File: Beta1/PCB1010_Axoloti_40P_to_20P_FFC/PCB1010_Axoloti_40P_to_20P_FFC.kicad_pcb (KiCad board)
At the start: 2 copper layers, 109.2 x 26.7 mm, 25 parts, among them J1 Axoloti_40Pin, J2 FPC_20POS

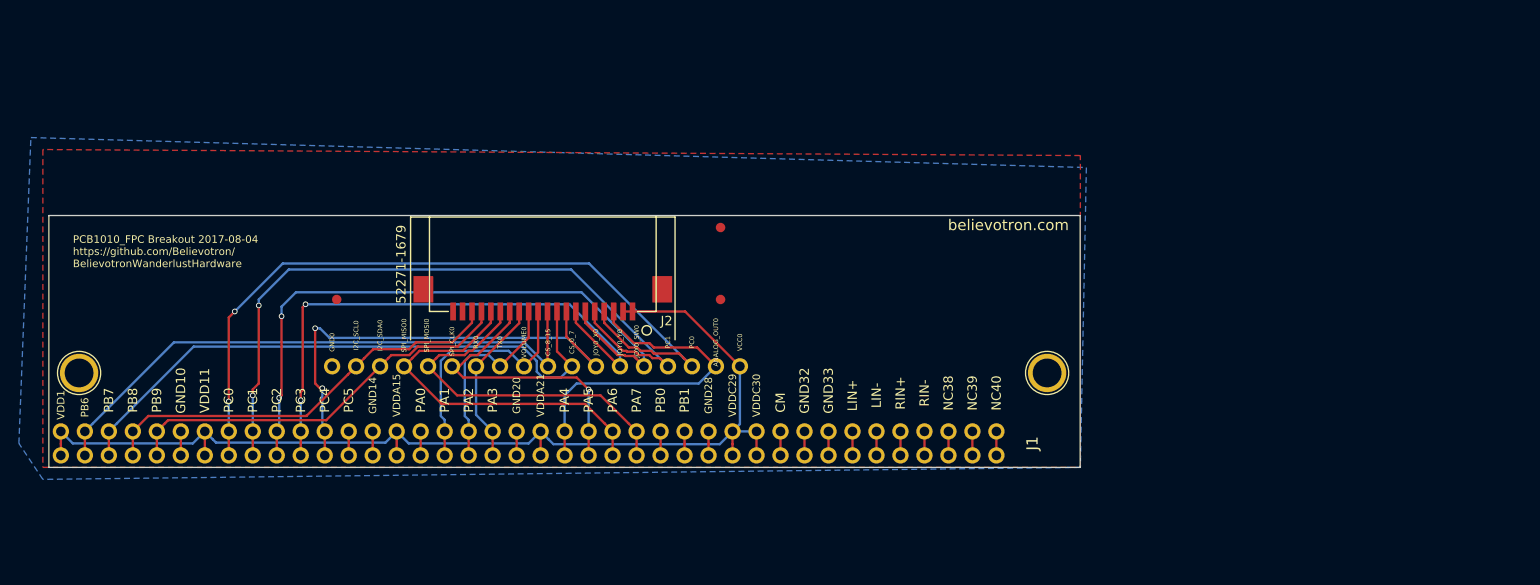
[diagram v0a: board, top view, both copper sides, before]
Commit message: Added TH connector, updated board outline
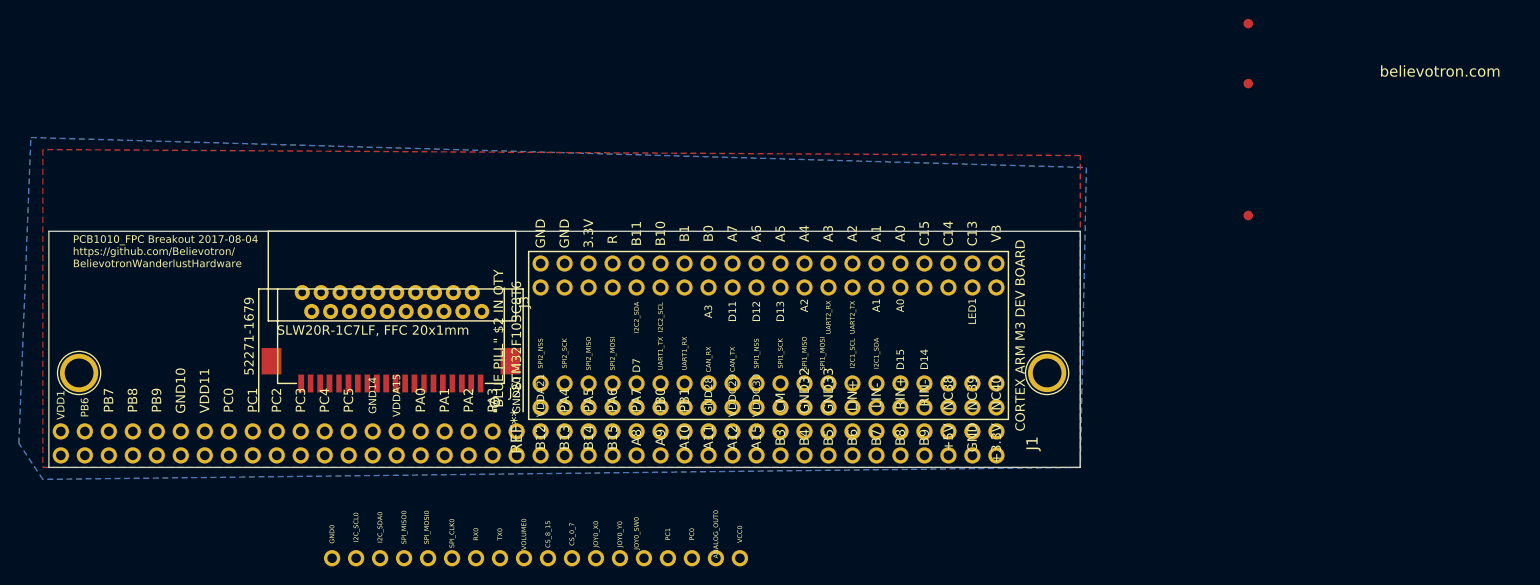
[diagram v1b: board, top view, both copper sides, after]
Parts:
- added J3: FPC_20POS, Liberry:FFC_20x1mm_SLW20R-1C7LF, F.Cu at (87.1, -16.5)
- added REF**: DIP-40_0, Liberry:BLUEPILL_CORTEXM3_STM32F103C8T6_THIN, F.Cu at (127.0, -14.0)
- moved REF** 96.9 mm to (177.8, -26.7)
- moved REF** 63.1 mm to (177.8, -47.0)
- moved REF** 57.9 mm to (177.8, -40.6)
- moved ANALOG_OUT0 20.3 mm to (121.4, 9.62)
- moved CS_0_7 20.3 mm to (106.2, 9.62)
- moved CS_8_15 20.3 mm to (103.7, 9.62)
- moved GND0 20.3 mm to (80.8, 9.62)
- moved I2C_SCL0 20.3 mm to (83.3, 9.62)
- moved I2C_SDA0 20.3 mm to (85.9, 9.62)
- moved JOY0_SW0 20.3 mm to (113.8, 9.62)
- moved JOY0_X0 20.3 mm to (108.7, 9.62)
- moved JOY0_Y0 20.3 mm to (111.3, 9.62)
- moved PC0 20.3 mm to (118.9, 9.62)
- moved PC1 20.3 mm to (116.4, 9.62)
- moved RX0 20.3 mm to (96.0, 9.62)
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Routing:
- net +3V3: track 115.1 -> 0.00 mm
- net /PC0: track 82.9 -> 0.00 mm, vias 2 -> 0
- net /PC1: track 76.5 -> 0.00 mm, vias 2 -> 0
- net /JOY0_SW: track 68.2 -> 0.00 mm, vias 2 -> 0
- net /CS_0_7: track 64.3 -> 0.00 mm
- net /CS_8_15: track 62.4 -> 0.00 mm
- net /JOY0_Y: track 60.7 -> 0.00 mm, vias 2 -> 0
- net /JOY0_X: track 52.5 -> 0.00 mm, vias 2 -> 0
- net /I2C_SCL: track 44.4 -> 0.00 mm
- net /I2C_SDA: track 42.9 -> 0.00 mm
- net /SPI_MISO: track 39.8 -> 0.00 mm
- net /SPI_MOSI: track 38.2 -> 0.00 mm
- net /ANALOG_OUT: track 37.6 -> 0.00 mm
- net /SPI_CLK: track 31.7 -> 0.00 mm, vias 1 -> 0
- net /VOLUME: track 26.5 -> 0.00 mm
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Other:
- board size 109.2 x 26.7 mm -> 109.2 x 25 mm

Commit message: Added Bluepill to PCB1010 design. Layout complete. Ready to route.
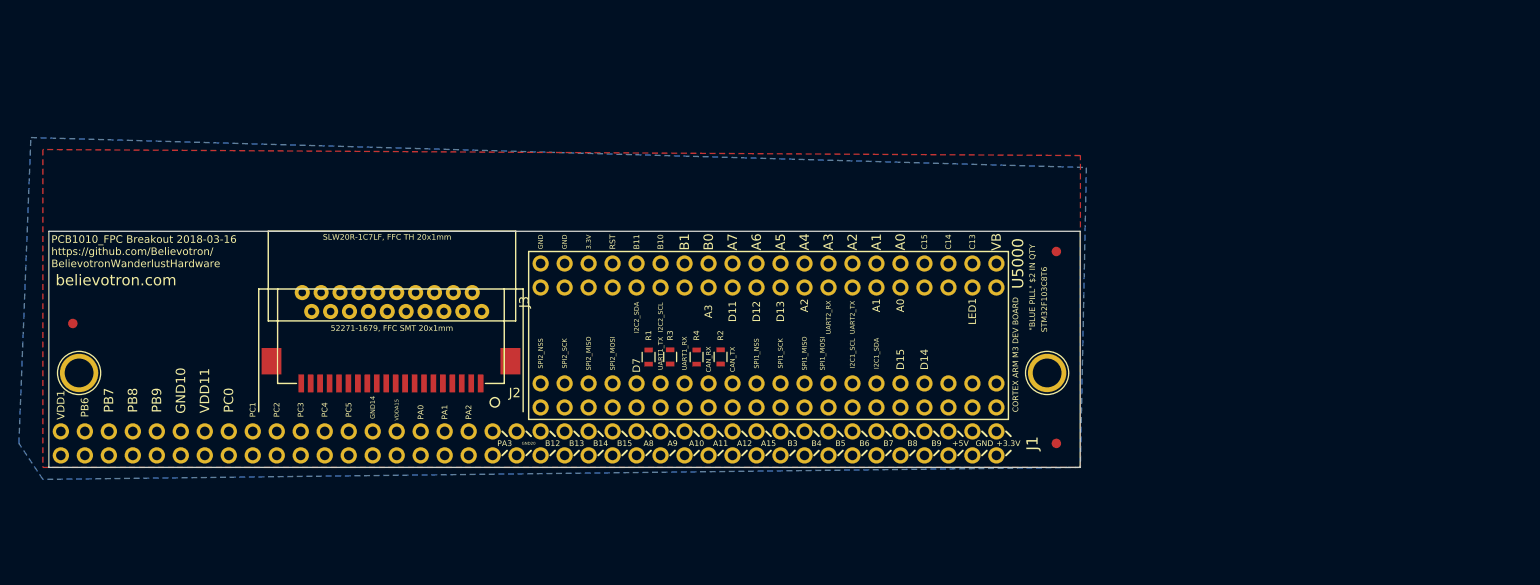
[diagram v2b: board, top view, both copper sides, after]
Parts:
- removed ANALOG_OUT0, CS_0_7, CS_8_15, GND0, I2C_SCL0, I2C_SDA0, JOY0_SW0, JOY0_X0, JOY0_Y0, PC0, PC1, RX0, SPI_CLK0, SPI_MISO0, SPI_MOSI0, TX0, VCC0, VOLUME0: CONN_01X01, Liberry:single_0.1
- added R1: 0, Resistors_SMD:R_0603, F.Cu at (114.3, -11.7)
- added R2: 0, Resistors_SMD:R_0603, F.Cu at (121.9, -11.7)
- added R3: 0, Resistors_SMD:R_0603, F.Cu at (116.6, -11.7)
- added R4: 0, Resistors_SMD:R_0603, F.Cu at (119.4, -11.7)
- U5000: renamed from REF**; value DIP-40_0 -> STM32F103C8T6_BLUE_PILL
- moved REF** 128.4 mm to (53.3, -15.2)
- moved REF** 31.5 mm to (157.5, -2.54)
- moved REF** 27.0 mm to (157.5, -22.9)
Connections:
- J1 pad 18: /TX -> /TX_AXO
- J1 pad 19: /RX -> /RX_AXO
- J1 pad 2: /CS_8_15 -> /CS_8_15_AXO
- J1 pad 23: /SPI_CLK -> /SPI_CLK_AXO
- J1 pad 24: /SPI_MISO -> /SPI_MISO_AXO
- J1 pad 25: /SPI_MOSI -> /SPI_MOSI_AXO
- J1 pad 3: /CS_0_7 -> /CS_0_7_AXO
- J1 pad 4: /I2C_SCL -> /I2C_SCL_AXO
- J1 pad 5: /I2C_SDA -> /I2C_SDA_AXO
- J1 pad 8: /PC0 -> /PC0_AXO
- J1 pad 9: /PC1 -> /PC1_AXO
- J2 pad 10: /CS_8_15 -> /CS_8_15_EXT
- J2 pad 12: /TX -> /TX_EXT
- J2 pad 13: /RX -> /RX_EXT
- J2 pad 14: /SPI_CLK -> /SPI_CLK_EXT
- J2 pad 15: /SPI_MOSI -> /SPI_MOSI_EXT
- J2 pad 16: /SPI_MISO -> /SPI_MISO_EXT
- J2 pad 17: /I2C_SDA -> /I2C_SDA_EXT
- J2 pad 18: /I2C_SCL -> /I2C_SCL_EXT
- J2 pad 4: /PC0 -> /PC0_EXT
- J2 pad 5: /PC1 -> /PC1_EXT
- J2 pad 9: /CS_0_7 -> /CS_0_7_EXT
- J3 pad 10: /CS_8_15 -> /CS_8_15_EXT
- J3 pad 12: /TX -> /TX_EXT
- J3 pad 13: /RX -> /RX_EXT
- J3 pad 14: /SPI_CLK -> /SPI_CLK_EXT
- J3 pad 15: /SPI_MOSI -> /SPI_MOSI_EXT
- J3 pad 16: /SPI_MISO -> /SPI_MISO_EXT
- J3 pad 17: /I2C_SDA -> /I2C_SDA_EXT
- J3 pad 18: /I2C_SCL -> /I2C_SCL_EXT
- J3 pad 4: /PC0 -> /PC0_EXT
- J3 pad 5: /PC1 -> /PC1_EXT
- J3 pad 9: /CS_0_7 -> /CS_0_7_EXT
- U5000 pad 3.3V: (no net) -> +3V3
- U5000 pad 5V: (no net) -> Net-(U5000-Pad5V)
- U5000 pad A0: (no net) -> /PC0_EXT
- U5000 pad A1: (no net) -> /PC1_EXT
- U5000 pad A10: (no net) -> Net-(R2-Pad1)
- U5000 pad A11: (no net) -> Net-(U5000-PadA11)
- U5000 pad A12: (no net) -> Net-(U5000-PadA12)
- U5000 pad A15: (no net) -> /CS_0_7_AXO
- U5000 pad A2: (no net) -> /UART_TX_EXT
- U5000 pad A3: (no net) -> /UART_RX_EXT
- U5000 pad A4: (no net) -> Net-(U5000-PadA4)
- U5000 pad A5: (no net) -> /CS_8_15_AXO
- U5000 pad A6: (no net) -> /CS_8_15_EXT
- U5000 pad A7: (no net) -> Net-(U5000-PadA7)
- U5000 pad A8: (no net) -> Net-(U5000-PadA8)
- U5000 pad A9: (no net) -> Net-(R1-Pad1)
- U5000 pad B0: (no net) -> Net-(U5000-PadB0)
- U5000 pad B1: (no net) -> Net-(U5000-PadB1)
- U5000 pad B10: (no net) -> /I2C_SCL_EXT
- U5000 pad B11: (no net) -> /I2C_SDA_EXT
- U5000 pad B12: (no net) -> /CS_0_7_EXT
- U5000 pad B13: (no net) -> /SPI_CLK_EXT
- U5000 pad B14: (no net) -> /SPI_MISO_EXT
- U5000 pad B15: (no net) -> /SPI_MOSI_EXT
- U5000 pad B3: (no net) -> /SPI_CLK_AXO
- U5000 pad B4: (no net) -> /SPI_MISO_AXO
- U5000 pad B5: (no net) -> /SPI_MOSI_AXO
- U5000 pad B6: (no net) -> /I2C_SCL_AXO
- U5000 pad B7: (no net) -> /I2C_SDA_AXO
- U5000 pad B8: (no net) -> Net-(U5000-PadB8)
- U5000 pad B9: (no net) -> Net-(U5000-PadB9)
- U5000 pad C13: (no net) -> Net-(U5000-PadC13)
- U5000 pad C14: (no net) -> /PC0_AXO
- U5000 pad C15: (no net) -> /PC1_AXO
- U5000 pad GND: (no net) -> GND
- U5000 pad R: (no net) -> /RESET
- U5000 pad VB: (no net) -> Net-(U5000-PadVB)
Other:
- board text added: "PCB1010_FPC Breakout 2018-03-16 https://github.com/Believotron/ BelievotronWanderlustHardware"
- board text removed: "PCB1010_FPC Breakout 2017-08-04 https://github.com/Believotron/ BelievotronWanderlustHardware"

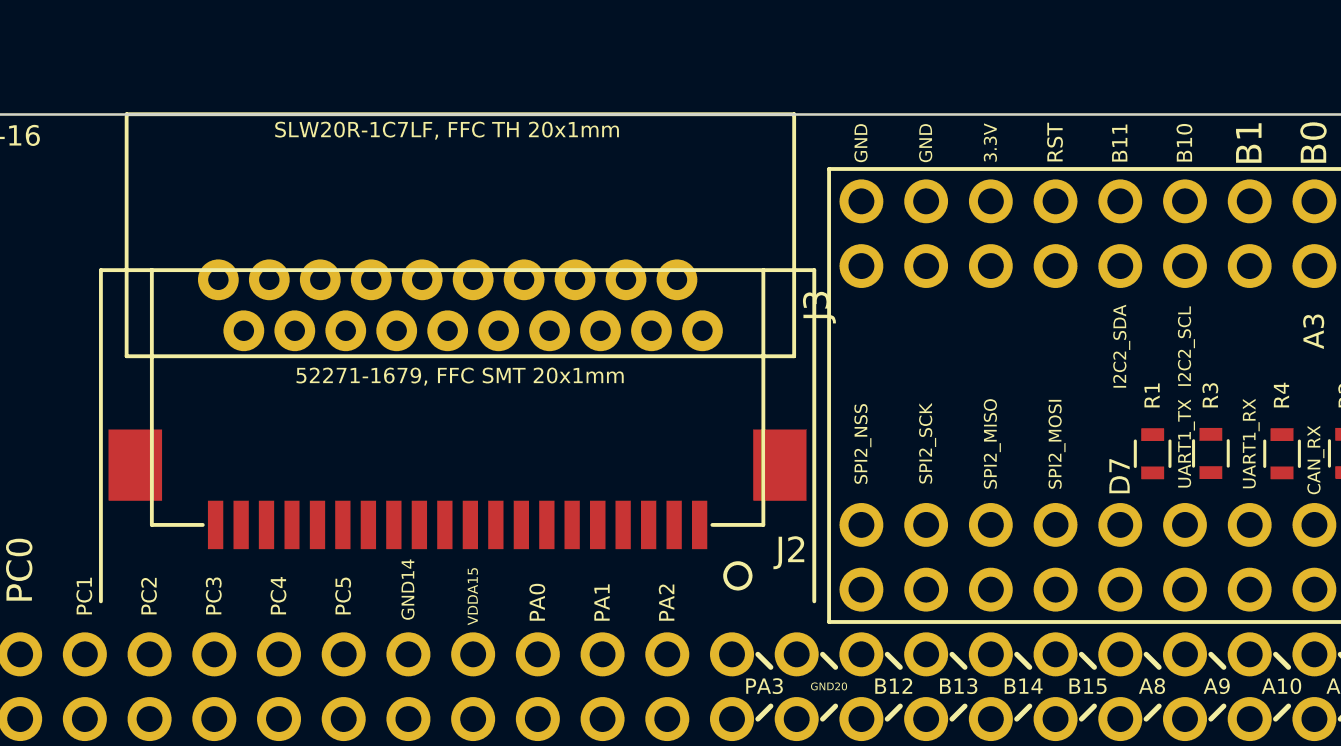
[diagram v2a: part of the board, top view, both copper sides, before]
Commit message: Corrected serial UART RX/TX nets
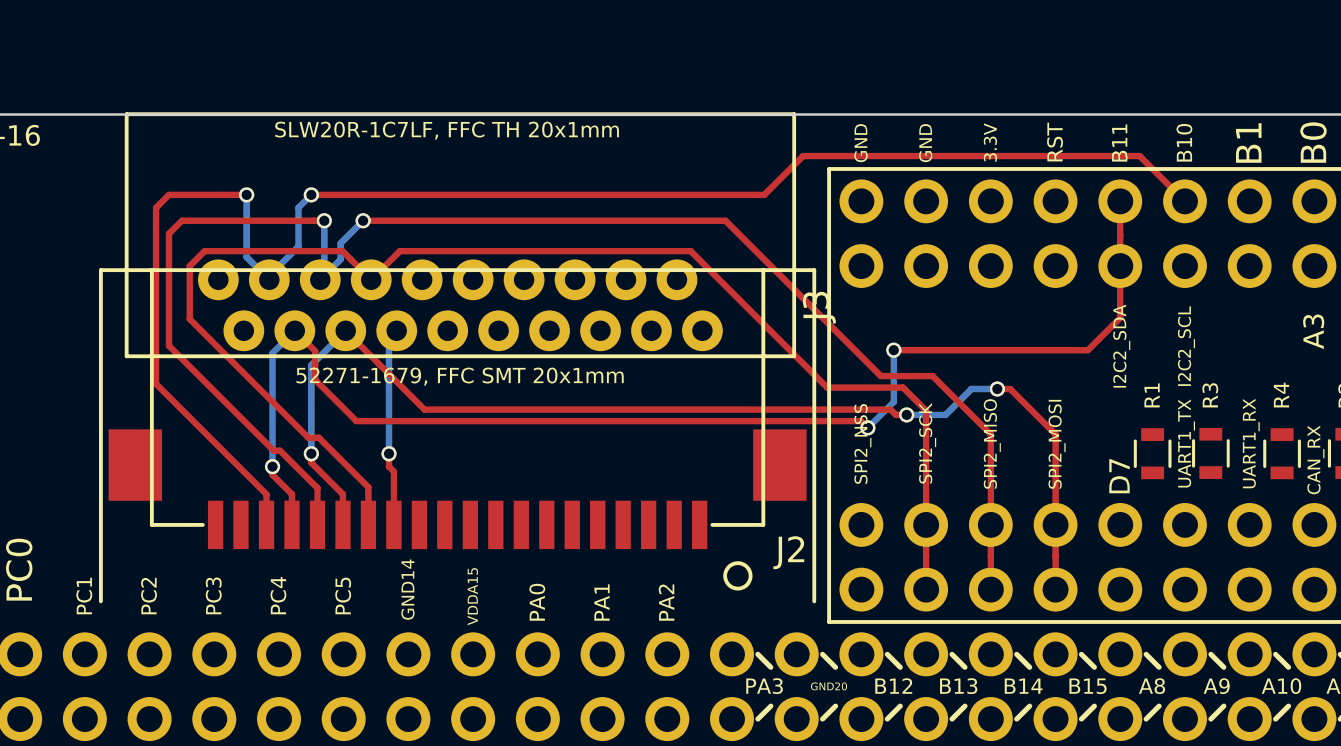
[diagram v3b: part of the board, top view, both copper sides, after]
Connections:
- net Net-(R2-Pad1) renamed /RX_BLUE_PILL
- U5000 pad A2: /UART_TX_EXT -> /TX_EXT
- U5000 pad A3: /UART_RX_EXT -> /RX_EXT
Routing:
- net /I2C_SCL_EXT: track 0.00 -> 61.4 mm, vias 0 -> 2
- net /SPI_MISO_EXT: track 0.00 -> 59.9 mm, vias 0 -> 2
- net /SPI_CLK_EXT: track 0.00 -> 53.0 mm
- net /I2C_SDA_EXT: track 0.00 -> 50.5 mm, vias 0 -> 3
- net /SPI_MOSI_EXT: track 0.00 -> 45.2 mm, vias 0 -> 3
- net /RX_EXT: track 0.00 -> 7.82 mm, vias 0 -> 1

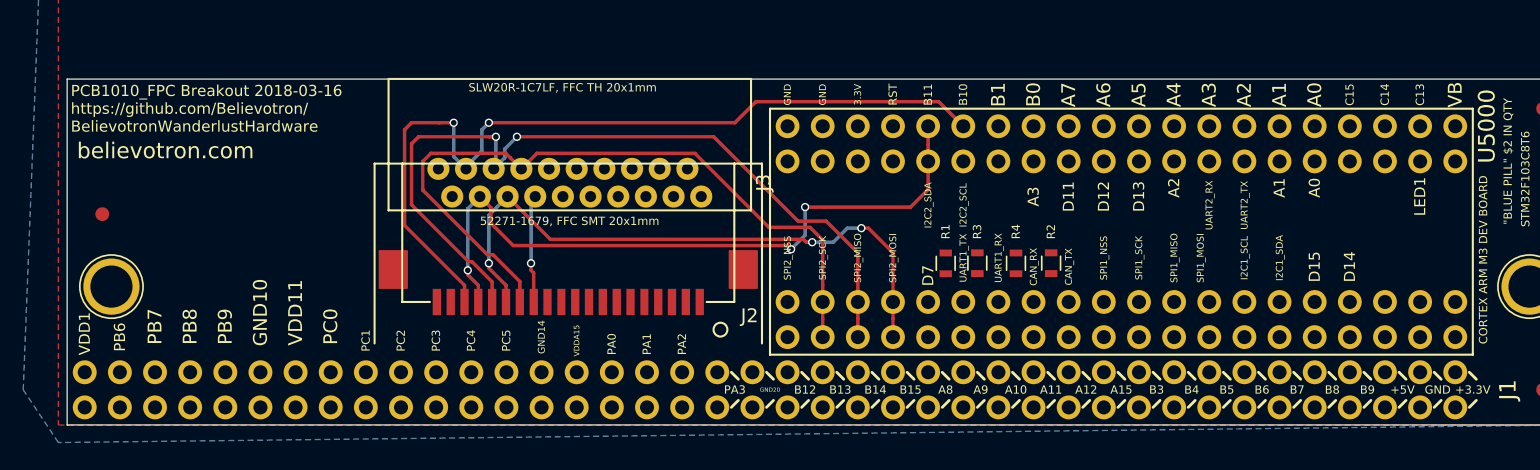
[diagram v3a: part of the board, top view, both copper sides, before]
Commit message: Routed all traces on PCB1010, except VCC and GND
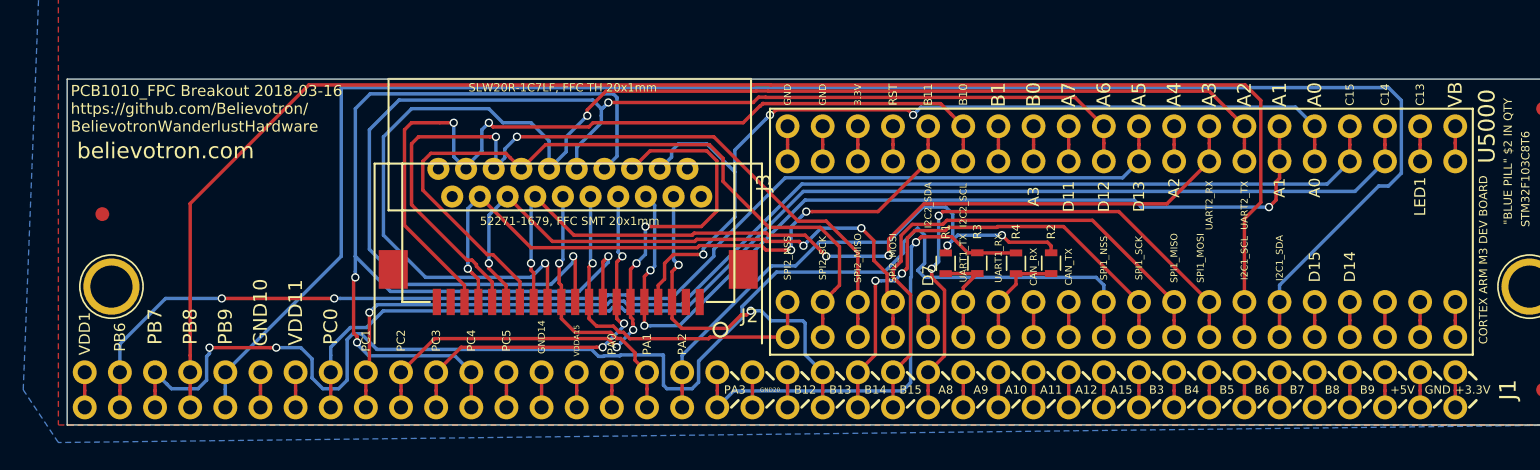
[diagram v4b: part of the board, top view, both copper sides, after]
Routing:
- net /I2C_SDA_AXO: track 0.00 -> 124.8 mm
- net /I2C_SCL_AXO: track 0.00 -> 113.7 mm
- net /CS_0_7_AXO: track 0.00 -> 96.8 mm, vias 0 -> 2
- net /TX_EXT: track 0.00 -> 96.2 mm, vias 0 -> 2
- net /CS_8_15_EXT: track 0.00 -> 91.9 mm, vias 0 -> 2
- net /PC0_AXO: track 0.00 -> 88.9 mm
- net /CS_8_15_AXO: track 0.00 -> 86.8 mm, vias 0 -> 2
- net /PC1_AXO: track 0.00 -> 85.1 mm, vias 0 -> 1
- net /JOY0_X: track 0.00 -> 77.9 mm, vias 0 -> 3
- net /PC0_EXT: track 0.00 -> 68.4 mm, vias 0 -> 3
- net /PC1_EXT: track 0.00 -> 65.2 mm, vias 0 -> 3
- net /RX_EXT: track 7.82 -> 64.5 mm, vias 1 -> 3
- net /JOY0_SW: track 0.00 -> 45.3 mm, vias 0 -> 4
- net /SPI_MOSI_AXO: track 0.00 -> 39.9 mm, vias 0 -> 2
- net /TX_AXO: track 0.00 -> 39.2 mm, vias 0 -> 2
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
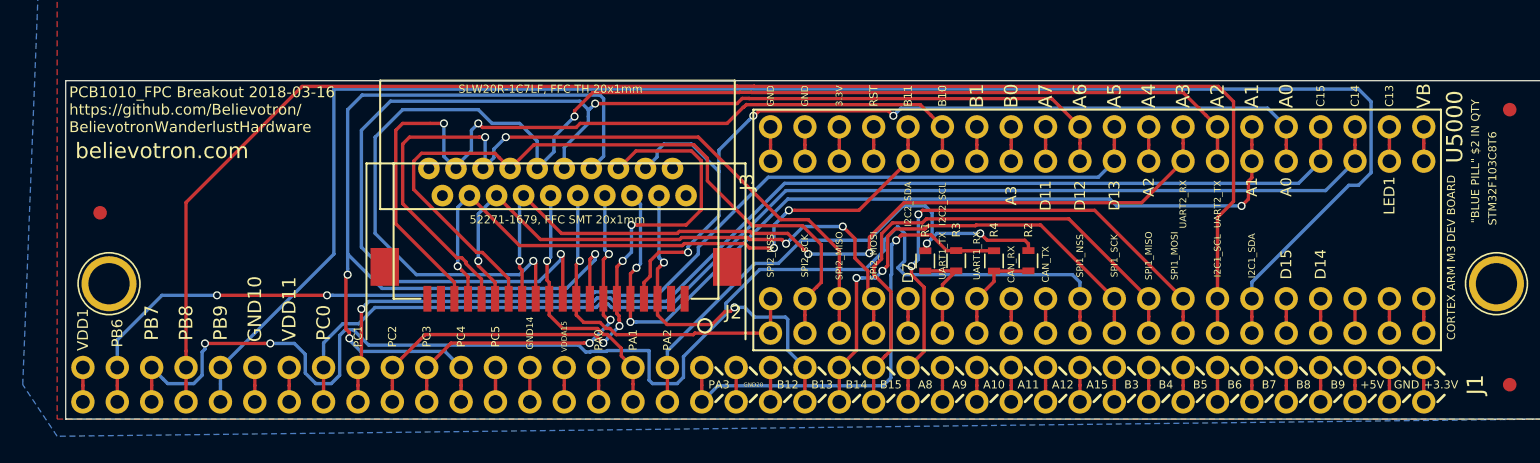
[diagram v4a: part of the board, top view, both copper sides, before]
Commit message: Fully routed. WIP. Waiting on DFM review.
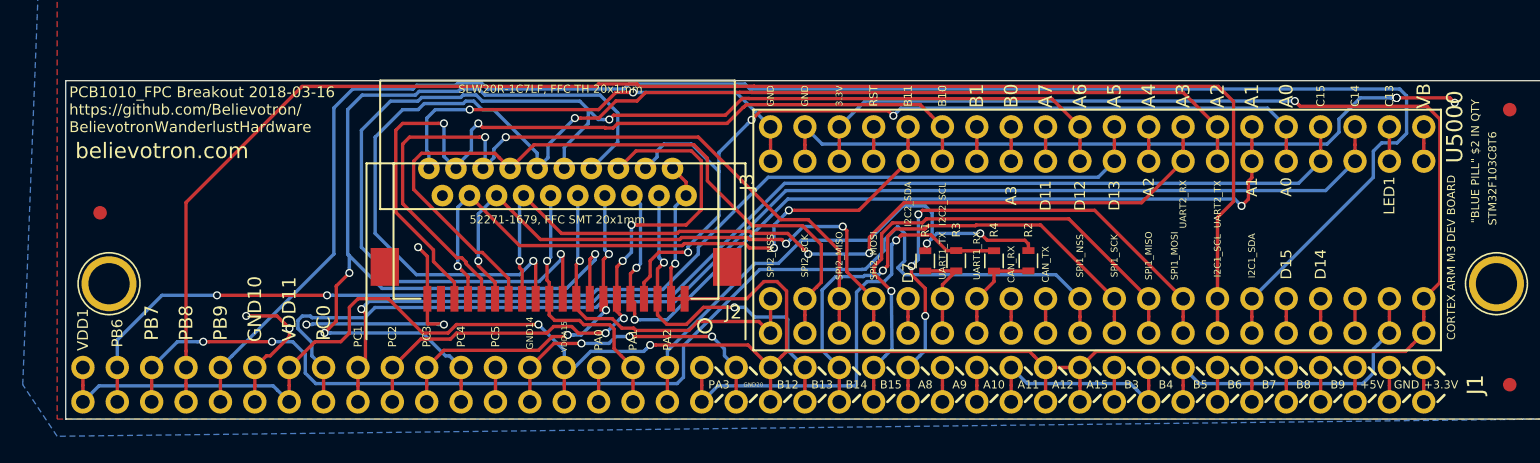
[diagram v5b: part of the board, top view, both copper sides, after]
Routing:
- net +3V3: track 20.3 -> 215.1 mm, vias 0 -> 4
- net GND: track 22.9 -> 176.6 mm, vias 0 -> 13
- net /CS_0_7_AXO: track 96.8 -> 87.6 mm
- net /I2C_SDA_AXO: track 124.8 -> 128.8 mm
- net /PC0_AXO: track 88.9 -> 92.4 mm
- net /JOY0_X: track 77.9 -> 81.3 mm
- net /SPI_CLK_AXO: track 36.4 -> 38.4 mm, vias 2 -> 1
- net /JOY0_Y: track 27.5 -> 26.5 mm
- net /CS_8_15_EXT: track 91.9 -> 92.9 mm
- net /VOLUME: track 20.0 -> 20.6 mm
- net /SPI_MISO_AXO: track 38.9 -> 39.0 mm, vias 0 -> 1
- net /SPI_MOSI_AXO: vias 2 -> 3
